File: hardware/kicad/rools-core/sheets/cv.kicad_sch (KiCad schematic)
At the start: 0 parts

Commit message: Add QSPI settings persistence, CV calibration app, and CV output driver.
Co-authored-by: Cursor <cursoragent@cursor.com>
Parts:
- added C11, C12, C13, C18, C19: 100nF, symbol Device:C
- added C14, C15, C16, C17: 10nF, symbol Device:C
- added J_CV_1, J_CV_2, J_CV_3, J_CV_4, J_CV_OUT_1, J_CV_OUT_2, J_CV_OUT_3, J_CV_OUT_4: (no value), ES_Daisy_Patch_Rev8:PJ301M-12SLOT, symbol patch-eagle:EURO_JACK_PJ301M-12
- added R10, R12, R14, R15, R16, R17, R18, R23, R24, R25, R26, R27, R28, R29, R30, R8: 100k, symbol Device:R
- added R11, R13, R31, R32, R33, R34, R7, R9: 16.5k, symbol Device:R
- added R19, R20, R21, R22: 1K, symbol Device:R
- added R35: 2K, symbol Device:R
- added R5, R6: 4.7k, symbol Device:R
- added RV1, RV2, RV3, RV4: R_Potentiometer, symbol Device:R_Potentiometer
- added U3: MCP4728, Package_SO:MSOP-10_3x3mm_P0.5mm, symbol Analog_DAC:MCP4728
- added U4: TL074, symbol Amplifier_Operational:TL074
- added U5: MCP6004, symbol Amplifier_Operational:MCP6004
- added U6: LM4040DBZ-10, Package_TO_SOT_SMD:SOT-23, symbol Reference_Voltage:LM4040DBZ-10
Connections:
- net +12V: now also C12.2, U4.4 (V+)
- net -12V: now also C13.1, R35.2, U4.11 (V-)
- net GND: now also C11.2, C12.1, C13.2, C18.2, C19.2, J_CV_1.GND, J_CV_1.GND2 (GND), J_CV_1.SW (NORM), J_CV_1.SW2 (NORM), J_CV_2.GND, J_CV_2.GND2 (GND), J_CV_2.SW (NORM), J_CV_2.SW2 (NORM), J_CV_3.GND, J_CV_3.GND2 (GND), J_CV_3.SW (NORM), J_CV_3.SW2 (NORM), J_CV_4.GND, J_CV_4.GND2 (GND), J_CV_4.SW (NORM), J_CV_4.SW2 (NORM), J_CV_OUT_1.GND, J_CV_OUT_1.GND2 (GND), J_CV_OUT_2.GND, J_CV_OUT_2.GND2 (GND), J_CV_OUT_3.GND, J_CV_OUT_3.GND2 (GND), J_CV_OUT_4.GND, J_CV_OUT_4.GND2 (GND), RV1.3, RV2.3, RV3.3, RV4.3, U3.10 (VSS), U3.4 (~{LDAC}), U4.10 (+), U4.12 (+), U4.3 (+), U4.5 (+), U5.10 (+), U5.11 (V-), U5.12 (+), U5.3 (+), U5.5 (+), U6.1 (K)
- new net: J_CV_OUT_4.SW (NORM), J_CV_OUT_4.SW2 (NORM)
- new net: J_CV_OUT_4.TIP, J_CV_OUT_4.TIP2 (TIP), R22.2
- new net: R17.2, R21.1, U4.8
- new net: R11.2, R12.2, R17.1, U4.9 (-)
- new net: C15.1, R25.2, R26.2, R32.1, U5.6 (-)
- new net: C17.1, R29.2, R30.2, R34.1, U5.13 (-)
- new net: C16.1, R27.2, R28.2, R33.1, U5.9 (-)
- new net: J_CV_4.TIP, J_CV_4.TIP2 (TIP), R30.1
- new net: R13.2, R14.2, R18.1, U4.13 (-)
- new net: J_CV_1.TIP, J_CV_1.TIP2 (TIP), R24.1
- new net: C14.1, R23.2, R24.2, R31.1, U5.2 (-)
- new net: J_CV_OUT_2.SW (NORM), J_CV_OUT_2.SW2 (NORM)
- new net: J_CV_OUT_2.TIP, J_CV_OUT_2.TIP2 (TIP), R20.2
- new net: J_CV_2.TIP, J_CV_2.TIP2 (TIP), R26.1
- new net: J_CV_3.TIP, J_CV_3.TIP2 (TIP), R28.1
- new net: R10.2, R16.1, R9.2, U4.6 (-)
- new net: R16.2, R20.1, U4.7
- new net: R15.2, R19.1, U4.1
- new net: J_CV_OUT_1.TIP, J_CV_OUT_1.TIP2 (TIP), R19.2
- new net: R18.2, R22.1, U4.14
- new net: J_CV_OUT_3.SW (NORM), J_CV_OUT_3.SW2 (NORM)
- new net: J_CV_OUT_3.TIP, J_CV_OUT_3.TIP2 (TIP), R21.2
- new net: R15.1, R7.2, R8.2, U4.2 (-)
- new net: J_CV_OUT_1.SW (NORM), J_CV_OUT_1.SW2 (NORM)
- new net +3V3_A: C18.1, RV1.1, RV2.1, RV3.1, RV4.1, U5.4 (V+)
- new net +3V3_D: R5.1, R6.1
- new net +3V3_DAC: C11.1, U3.1 (VDD)
- new net -10V_REF: C19.1, R10.1, R12.1, R14.1, R23.1, R25.1, R27.1, R29.1, R35.1, R8.1, U6.2 (A)
- new net CV1_ADC: C14.2, R31.2, U5.1
- new net CV2_ADC: C15.2, R32.2, U5.7
- new net CV3_ADC: C17.2, R34.2, U5.14
- new net CV4_ADC: C16.2, R33.2, U5.8
- new net DAC_A: R7.1, U3.6 (VOUTA)
- new net DAC_B: R9.1, U3.7 (VOUTB)
- new net DAC_C: R11.1, U3.8 (VOUTC)
- new net DAC_D: R13.1, U3.9 (VOUTD)
- new net I2C1_SCL: R5.2, U3.2 (SCL)
- new net I2C1_SDA: R6.2, U3.3 (SDA)
- new net KNOB1_ADC: RV1.2
- new net KNOB2_ADC: RV2.2
- new net KNOB3_ADC: RV3.2
- new net KNOB4_ADC: RV4.2
- no-connect marks 0 -> 5
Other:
- note added: "J_CV_OUT_1 IN: 0V - 3.3V OUT: -10V - +10V"

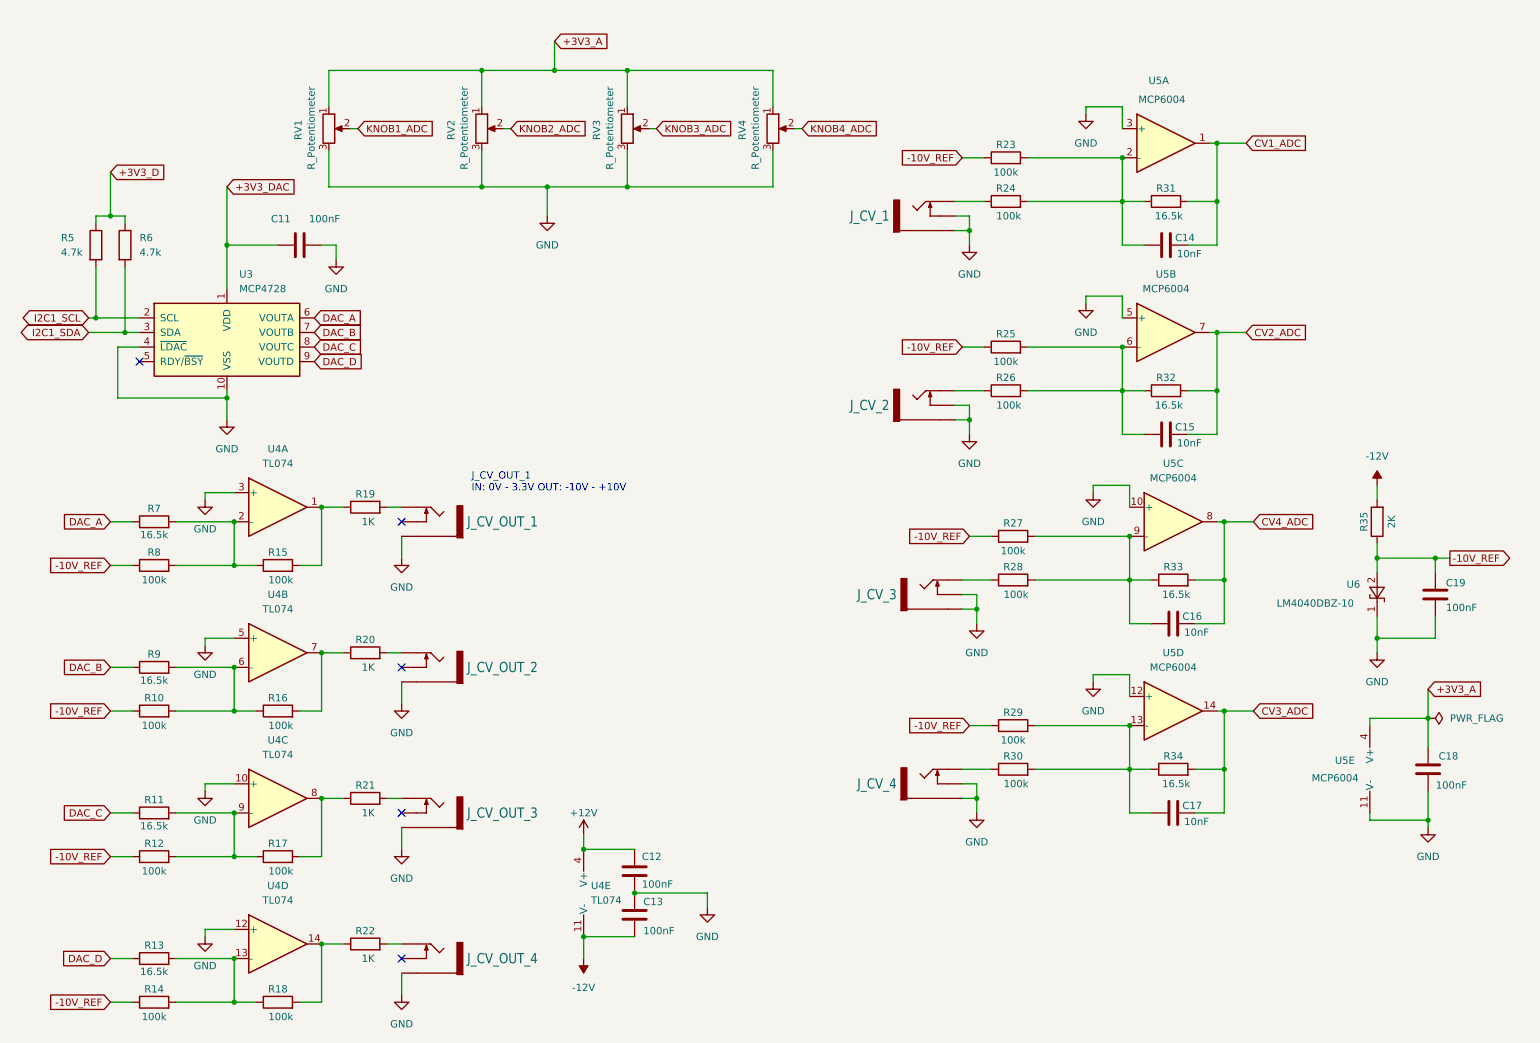
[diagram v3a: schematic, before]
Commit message: Sync Core schematic Rev 0.2 with docs and firmware.
Align DAC8565/OPA4171 CV path (2.5V internal ref, 12.5k/100k), LM393 power-fail hold-up, and SPI1 CV driver fixes (LDAC polarity, debounced save with backlight off).

Co-authored-by: Cursor <cursoragent@cursor.com>
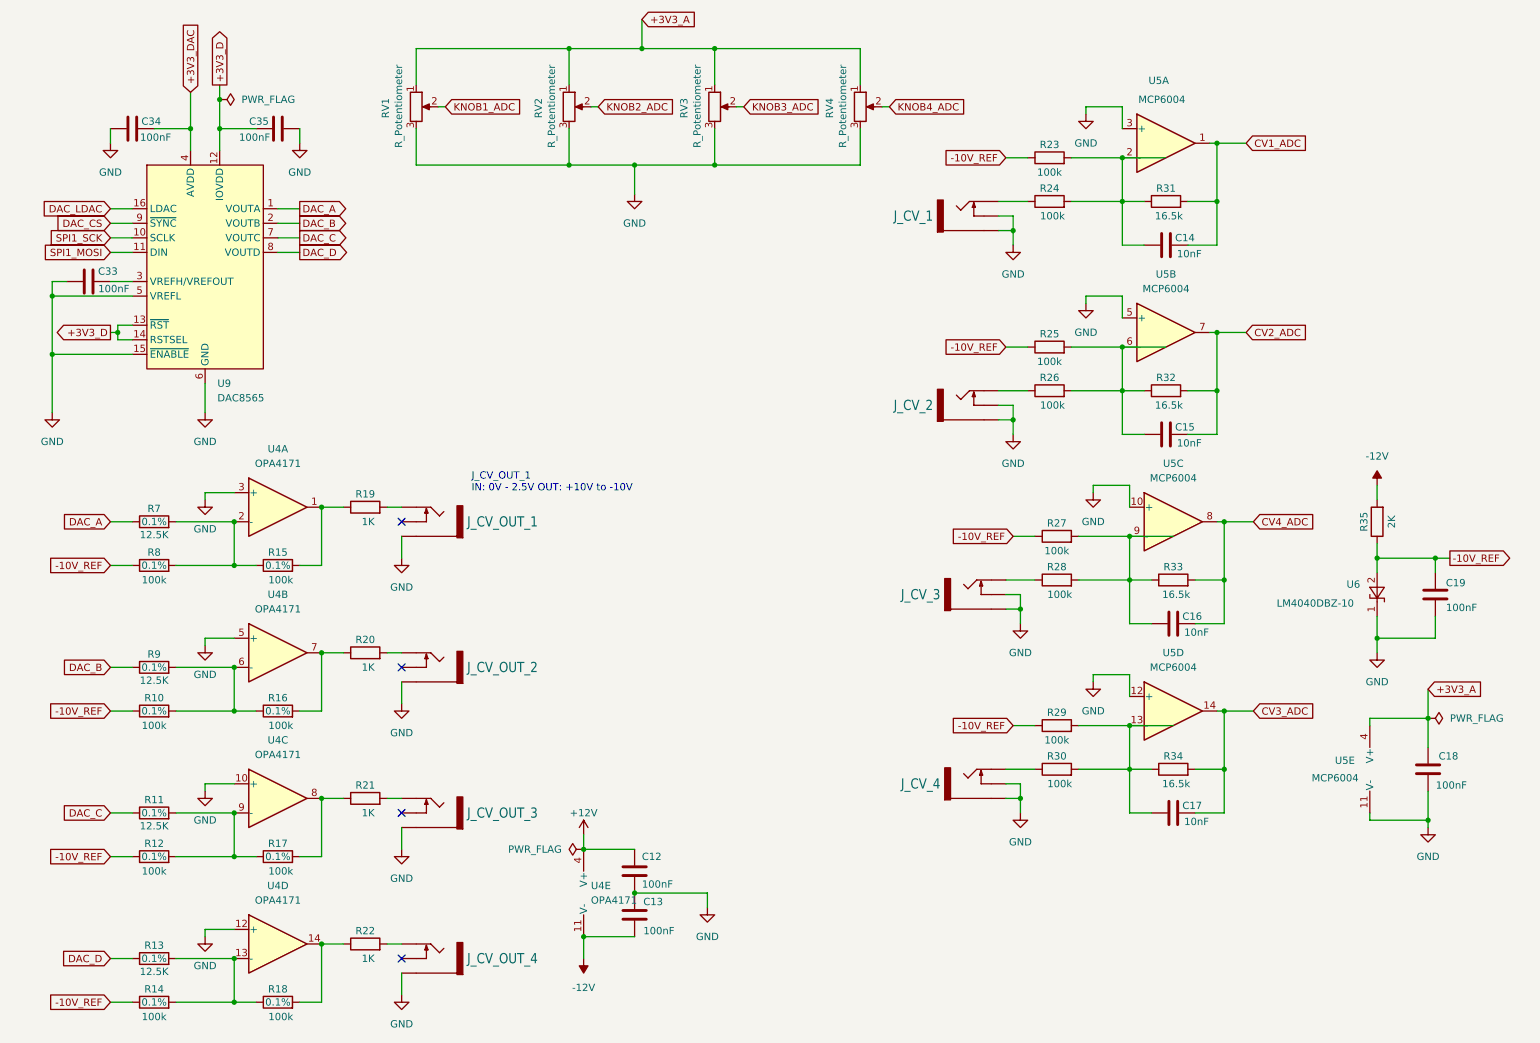
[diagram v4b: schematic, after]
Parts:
- removed C11: 100nF, symbol Device:C
- removed R5, R6: 4.7k, symbol Device:R
- removed U3: MCP4728, Package_SO:MSOP-10_3x3mm_P0.5mm, symbol Analog_DAC:MCP4728
- added C33, C34, C35: 100nF, symbol Device:C
- added U9: DAC8565, Package_SO:TSSOP-16_4.4x5mm_P0.65mm, symbol Analog_DAC:DAC8565
- R10, R12, R14, R15, R16, R17, R18, R8: Tolerance (none) -> 0.1%
- R11, R13, R7, R9: value 16.5k -> 12.5K; Tolerance (none) -> 0.1%
- U4: value TL074 -> OPA4171
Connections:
- net +3V3_D: now also C35.1, U9.12 (IOVDD), U9.13 (~{RST}), U9.14 (RSTSEL)
- net +3V3_DAC: now also C34.1, U9.4 (AVDD)
- net DAC_A: now also U9.1 (VOUTA)
- net DAC_B: now also U9.2 (VOUTB)
- net DAC_C: now also U9.7 (VOUTC)
- net DAC_D: now also U9.8 (VOUTD)
- net GND: now also C33.2, C34.2, C35.2, U9.15 (~{ENABLE}), U9.5 (VREFL), U9.6 (GND)
- new net: C33.1, U9.3 (VREFH/VREFOUT)
- new net DAC_CS: U9.9 (~{SYNC})
- new net DAC_LDAC: U9.16 (LDAC)
- new net SPI1_MOSI: U9.11 (DIN)
- new net SPI1_SCK: U9.10 (SCLK)
- no-connect marks 5 -> 4
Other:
- note added: "J_CV_OUT_1 IN: 0V - 2.5V OUT: +10V to -10V"
- note removed: "J_CV_OUT_1 IN: 0V - 3.3V OUT: -10V - +10V"
- moved on the sheet: J_CV_1, J_CV_2, J_CV_3, J_CV_4, R23, R24, R25, R26, R27, R28, R29, R30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

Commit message: Finalize Core schematic pin map and JLC BOM for assembly.
MIDI USART1 on D13/D14, DAC8565 on D26/D27, and document P2 EXP_BUS so Exp I/O no longer conflicts with CV Out.

Co-authored-by: Cursor <cursoragent@cursor.com>
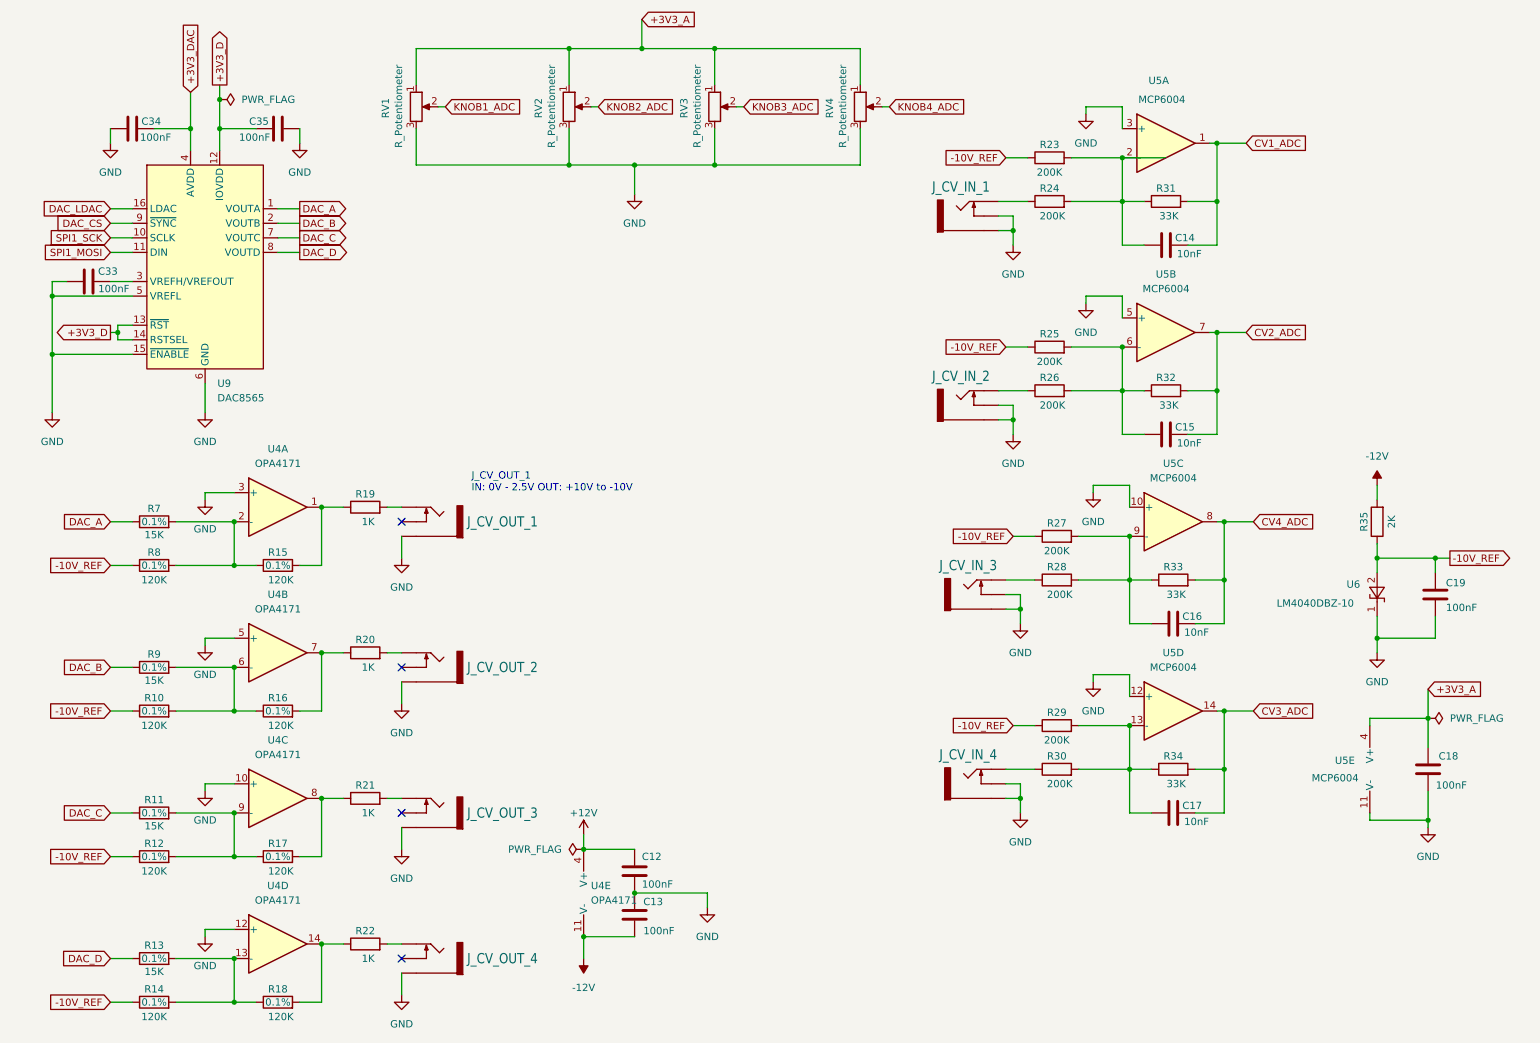
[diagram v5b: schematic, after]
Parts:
- C12, C13, C18, C19, C33, C34, C35: footprint (none) -> Capacitor_SMD:C_0603_1608Metric; LCSC (none) -> C14663
- C14, C15, C16, C17: footprint (none) -> Capacitor_SMD:C_0603_1608Metric; LCSC (none) -> C1710
- J_CV_IN_1: renamed from J_CV_1; footprint ES_Daisy_Patch_Rev8:PJ301M-12SLOT -> Connector_Audio:Jack_3.5mm_QingPu_WQP-PJ398SM_Vertical_CircularHoles
- J_CV_IN_2: renamed from J_CV_2; footprint ES_Daisy_Patch_Rev8:PJ301M-12SLOT -> Connector_Audio:Jack_3.5mm_QingPu_WQP-PJ398SM_Vertical_CircularHoles
- J_CV_IN_3: renamed from J_CV_3; footprint ES_Daisy_Patch_Rev8:PJ301M-12SLOT -> Connector_Audio:Jack_3.5mm_QingPu_WQP-PJ398SM_Vertical_CircularHoles
- J_CV_IN_4: renamed from J_CV_4; footprint ES_Daisy_Patch_Rev8:PJ301M-12SLOT -> Connector_Audio:Jack_3.5mm_QingPu_WQP-PJ398SM_Vertical_CircularHoles
- J_CV_OUT_1, J_CV_OUT_2, J_CV_OUT_3, J_CV_OUT_4: footprint ES_Daisy_Patch_Rev8:PJ301M-12SLOT -> Connector_Audio:Jack_3.5mm_QingPu_WQP-PJ398SM_Vertical_CircularHoles
- R10, R12, R14, R15, R16, R17, R18, R8: value 100k -> 120K; footprint (none) -> Resistor_SMD:R_0603_1608Metric; LCSC (none) -> C136959
- R11, R13, R7, R9: value 12.5K -> 15K; footprint (none) -> Resistor_SMD:R_0603_1608Metric; LCSC (none) -> C326733
- R19, R20, R21, R22: footprint (none) -> Resistor_SMD:R_0603_1608Metric; LCSC (none) -> C21190
- R23, R24, R25, R26, R27, R28, R29, R30: value 100k -> 200K; footprint (none) -> Resistor_SMD:R_0603_1608Metric; LCSC (none) -> C728585
- R31, R32, R33, R34: value 16.5k -> 33K; footprint (none) -> Resistor_SMD:R_0603_1608Metric; LCSC (none) -> C705768
- R35: footprint (none) -> Resistor_SMD:R_0603_1608Metric; LCSC (none) -> C21194
- RV1, RV2, RV3, RV4: footprint (none) -> Potentiometer_THT:Potentiometer_Alps_RK09L_Single_Vertical
- U4: footprint (none) -> Package_SO:SOIC-14_3.9x8.7mm_P1.27mm; LCSC (none) -> C46269
- U5: footprint (none) -> Package_SO:SOIC-14_3.9x8.7mm_P1.27mm; LCSC (none) -> C7378
- U6: LCSC (none) -> C201738
- U9: LCSC (none) -> C69596

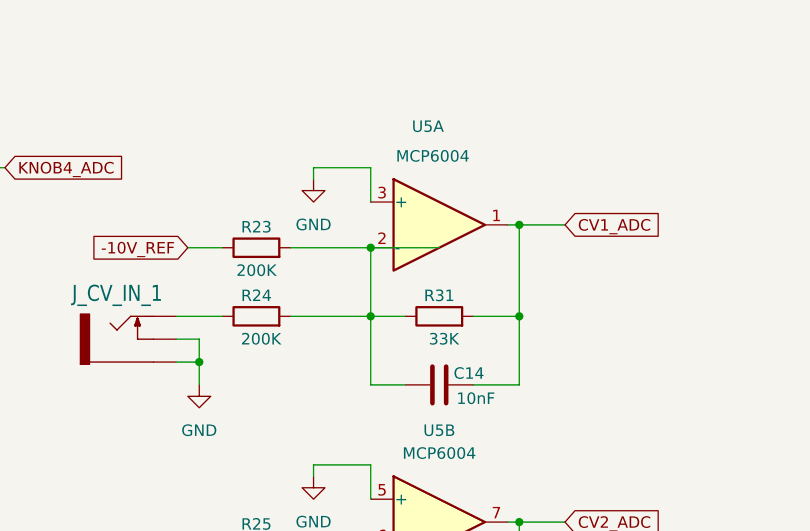
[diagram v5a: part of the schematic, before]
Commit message: Use Patch ENCODERNOSILK symbols for EC11 encoders on UI sheet.
Co-authored-by: Cursor <cursoragent@cursor.com>
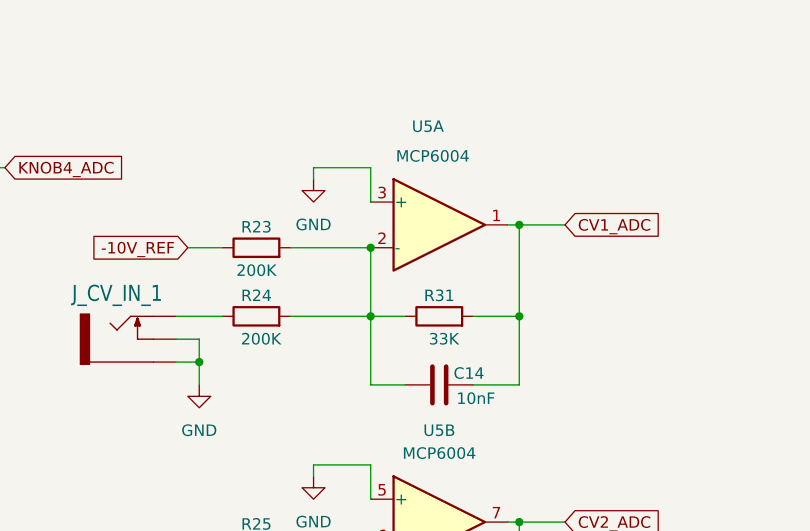
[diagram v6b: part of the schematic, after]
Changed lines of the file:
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@@
-	(wire
-		(pts
-			(xy 218.44 41.91) (xy 210.82 41.91)
-		)
-		(stroke
-			(width 0)
-			(type default)
-		)
-	)
 	(wire
 		(pts
